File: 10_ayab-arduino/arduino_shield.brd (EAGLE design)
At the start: 69.9 x 54.6 mm, 23 parts, among them IC3 PCF8574T, IC4 PCF8574T

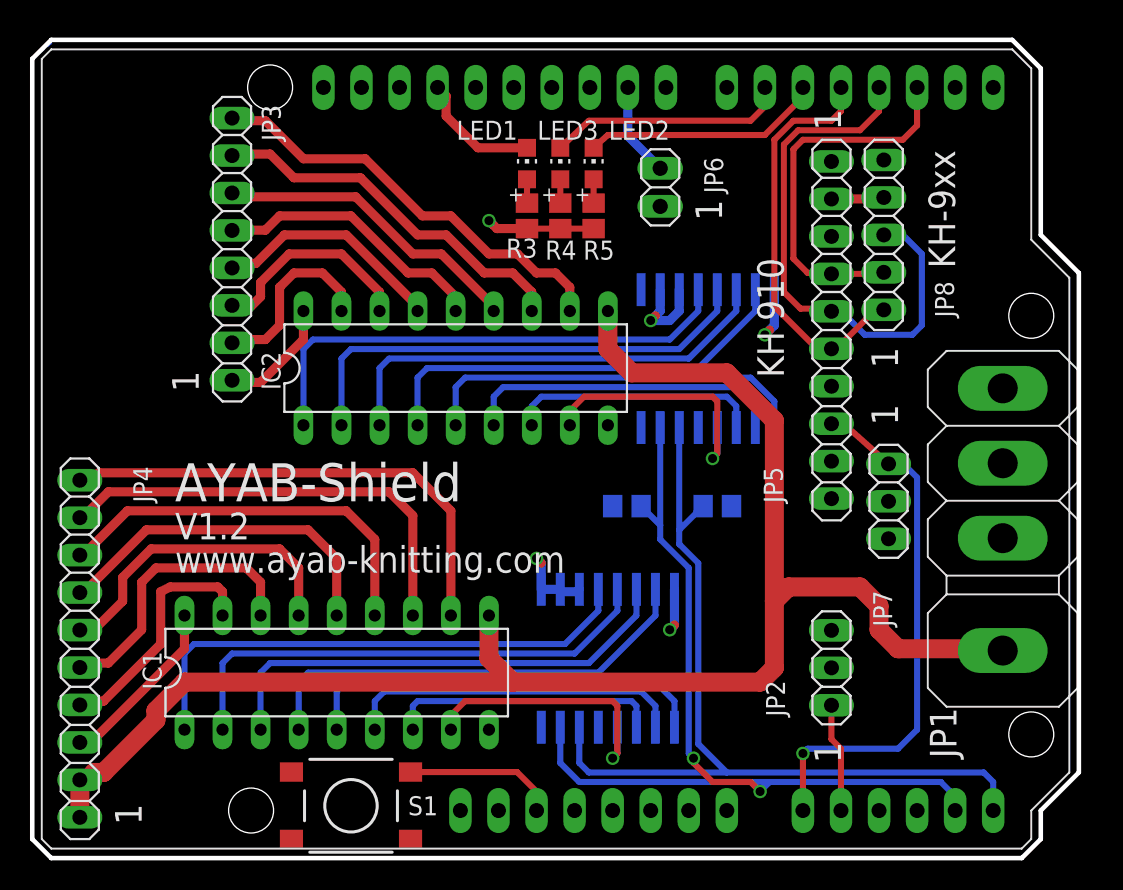
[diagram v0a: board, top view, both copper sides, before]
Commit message: Created a shield version without SMD-Parts
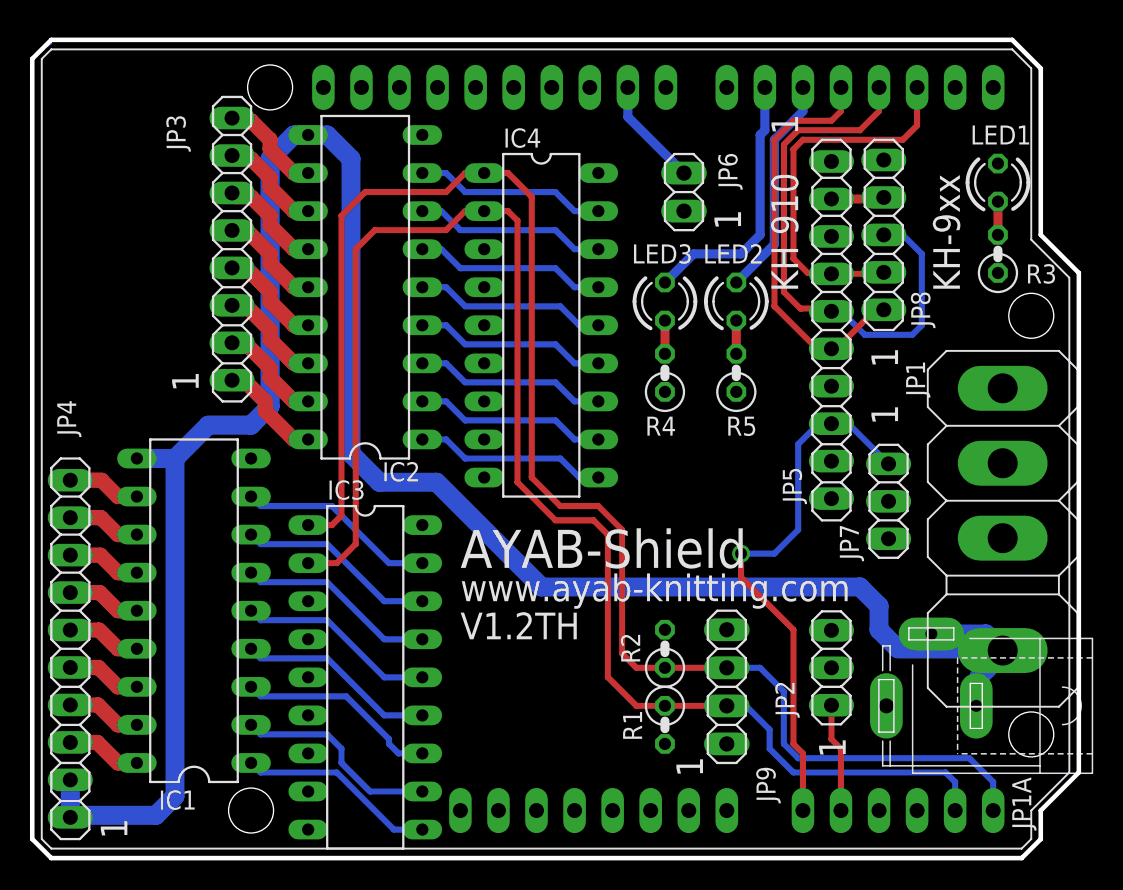
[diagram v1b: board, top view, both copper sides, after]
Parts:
- removed S1: DTSM-6, switch-tact:DTSM-6
- added JP1A: (no value), con-jack:SPC4078
- added JP9: (no value), pinhead:1X04
- IC3, IC4: value PCF8574T -> MCP2300X/P; device micro-philips:SO16W -> adafruit:DIL18
- LED1, LED2, LED3: device adafruit:CHIP-LED0805 -> led:LED3MM
- R1, R2: device rcl:R0805 -> rcl:0207/2V
- R3, R4, R5: device resistor:R0805 -> rcl:0207/2V
- moved R3 31.5 mm to (63.8, 39.7), turned to 90 degrees
- moved LED1 31.5 mm to (63.8, 44.5), turned to 90 degrees
- moved IC3 16.2 mm to (21.6, 11.4), flipped to the top, turned to 270 degrees
- moved R1 14.8 mm to (41.6, 8.26), flipped to the top, turned to 270 degrees
- moved R5 14.2 mm to (46.4, 31.8)
- moved LED2 13.2 mm to (46.4, 36.5), turned to 90 degrees
- moved R4 12.6 mm to (41.6, 31.8)
- moved LED3 11.6 mm to (41.6, 36.5), turned to 90 degrees
- moved IC4 11.3 mm to (33.3, 34.9), flipped to the top, turned to 270 degrees
- moved IC1 10.4 mm to (10.2, 15.9), turned to 90 degrees
- moved R2 10.1 mm to (41.6, 13.3), flipped to the top, turned to 90 degrees
- moved IC2 8.09 mm to (21.6, 37.5), turned to 90 degrees
- moved JP6 1.62 mm to (42.9, 43.8)
- moved JP4 0.64 mm to (1.91, 13.3)
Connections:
- net +15V: now also JP1A.1, JP1A.2
- net +5V: now also IC3.18, IC3.6, IC4.18, IC4.5, IC4.6, JP9.1, R3.1; no longer IC3.16, IC4.1, IC4.16, R3.2
- net GND: now also IC3.4, IC3.5, IC3.9, IC4.4, IC4.9, JP1A.3, JP9.4, LED1.K; no longer IC3.1, IC3.2, IC3.8, IC4.2, IC4.8, LED1.C, S1.4
- net N$1: now also IC4.10; no longer IC4.4
- net N$10: now also IC4.11; no longer IC4.5
- net N$11: now also IC4.12; no longer IC4.6
- net N$12: now also IC4.13; no longer IC4.7
- net N$13: now also IC4.14; no longer IC4.9
- net N$14: now also IC4.15; no longer IC4.10
- net N$15: now also IC4.16; no longer IC4.11
- net N$16: now also IC4.17; no longer IC4.12
- net N$2: now also IC3.10; no longer IC3.4
- net N$3: now also IC3.11; no longer IC3.5
- net N$33: now also R3.2; no longer R3.1
- net N$35: now also LED3.K; no longer LED3.C
- net N$36: now also LED2.K; no longer LED2.C
- net N$4: now also IC3.12; no longer IC3.6
- net N$5: now also IC3.13; no longer IC3.7
- net N$6: now also IC3.14; no longer IC3.9
- net N$7: now also IC3.15; no longer IC3.10
- net N$8: now also IC3.16; no longer IC3.11
- net N$9: now also IC3.17; no longer IC3.12
- net RESET: no longer S1.2
- net SCL: now also IC3.1, IC4.1, JP9.3; no longer IC3.14, IC4.14
- net SDA: now also IC3.2, IC4.2, JP9.2; no longer IC3.15, IC4.15
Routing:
- net SCL: track 59.0 -> 103.8 mm
- net +15V: track 107.9 -> 145.3 mm
- net SDA: track 61.9 -> 98.7 mm, vias 2 -> 0
- net N$25: track 33.0 -> 4.90 mm
- net GND: track 30.7 -> 3.53 mm, vias 4 -> 0
- net N$26: track 30.6 -> 4.91 mm
- net N$27: track 27.2 -> 4.93 mm
- net N$2: track 35.3 -> 13.3 mm
- net N$24: track 28.8 -> 6.97 mm
- net N$1: track 33.9 -> 12.8 mm
- net N$3: track 33.7 -> 13.8 mm
- net N$10: track 32.3 -> 12.8 mm
- net N$4: track 32.2 -> 13.5 mm
- net N$28: track 23.5 -> 4.95 mm
- net N$23: track 25.1 -> 6.99 mm
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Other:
- board text added: "V1.2TH"
- board text removed: "V1.2"

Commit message: Finalization of AYAB Shield 1.3 Through Hole
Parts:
- removed JP1A: (no value), con-jack:SPC4078
- removed U$1: (no value), frames:A4L-LOC
- added U$2: V1.3TH, frames:A4L-LOC
- added X1: NEB1R, con-lumberg:NEB1R
- moved JP2 17.6 mm to (35.2, 9.53)
- moved R1 16.0 mm to (32.7, 21.6), turned to 180 degrees
- moved R2 8.35 mm to (40.3, 21.6), turned to 0 degrees
- moved JP9 0.38 mm to (45.3, 10.8)
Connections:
- net +15V: now also X1.2, X1.3; no longer JP1A.1, JP1A.2
- net GND: now also X1.1@1; no longer JP1A.3
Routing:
- net EOL0L: track 7.29 -> 21.5 mm
- net GND: track 3.53 -> 8.35 mm
- net +15V: track 145.3 -> 142.0 mm
- net SDA: track 98.7 -> 99.9 mm
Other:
- board text added: "+"
- board text added: "-"
- board text added: "5V"
- board text added: "GND"
- board text added: "SCL"
- board text added: "SDA"
- board text added: "V1.3TH"
- board text removed: "V1.2TH"
